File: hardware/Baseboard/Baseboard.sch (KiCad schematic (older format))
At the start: 0 parts

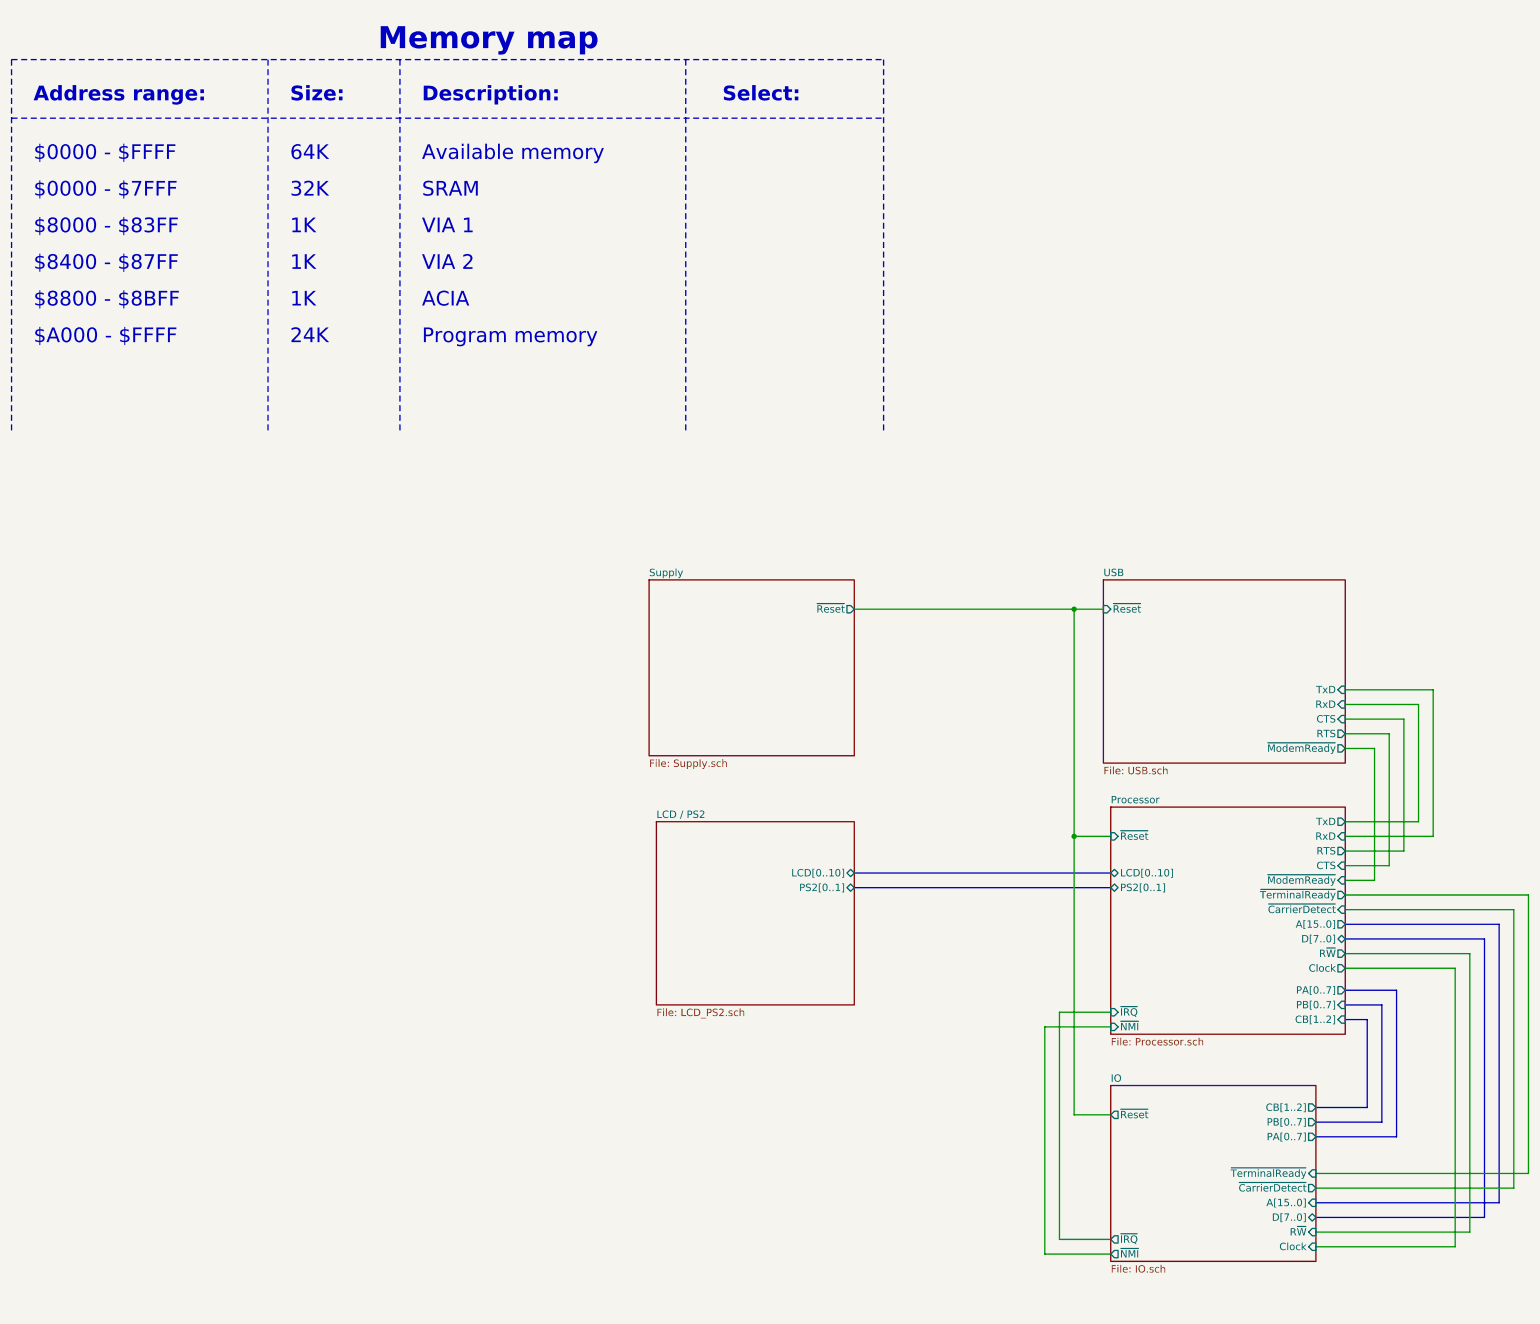
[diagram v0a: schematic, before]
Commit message: Rework hardware for IRQ, change some routing
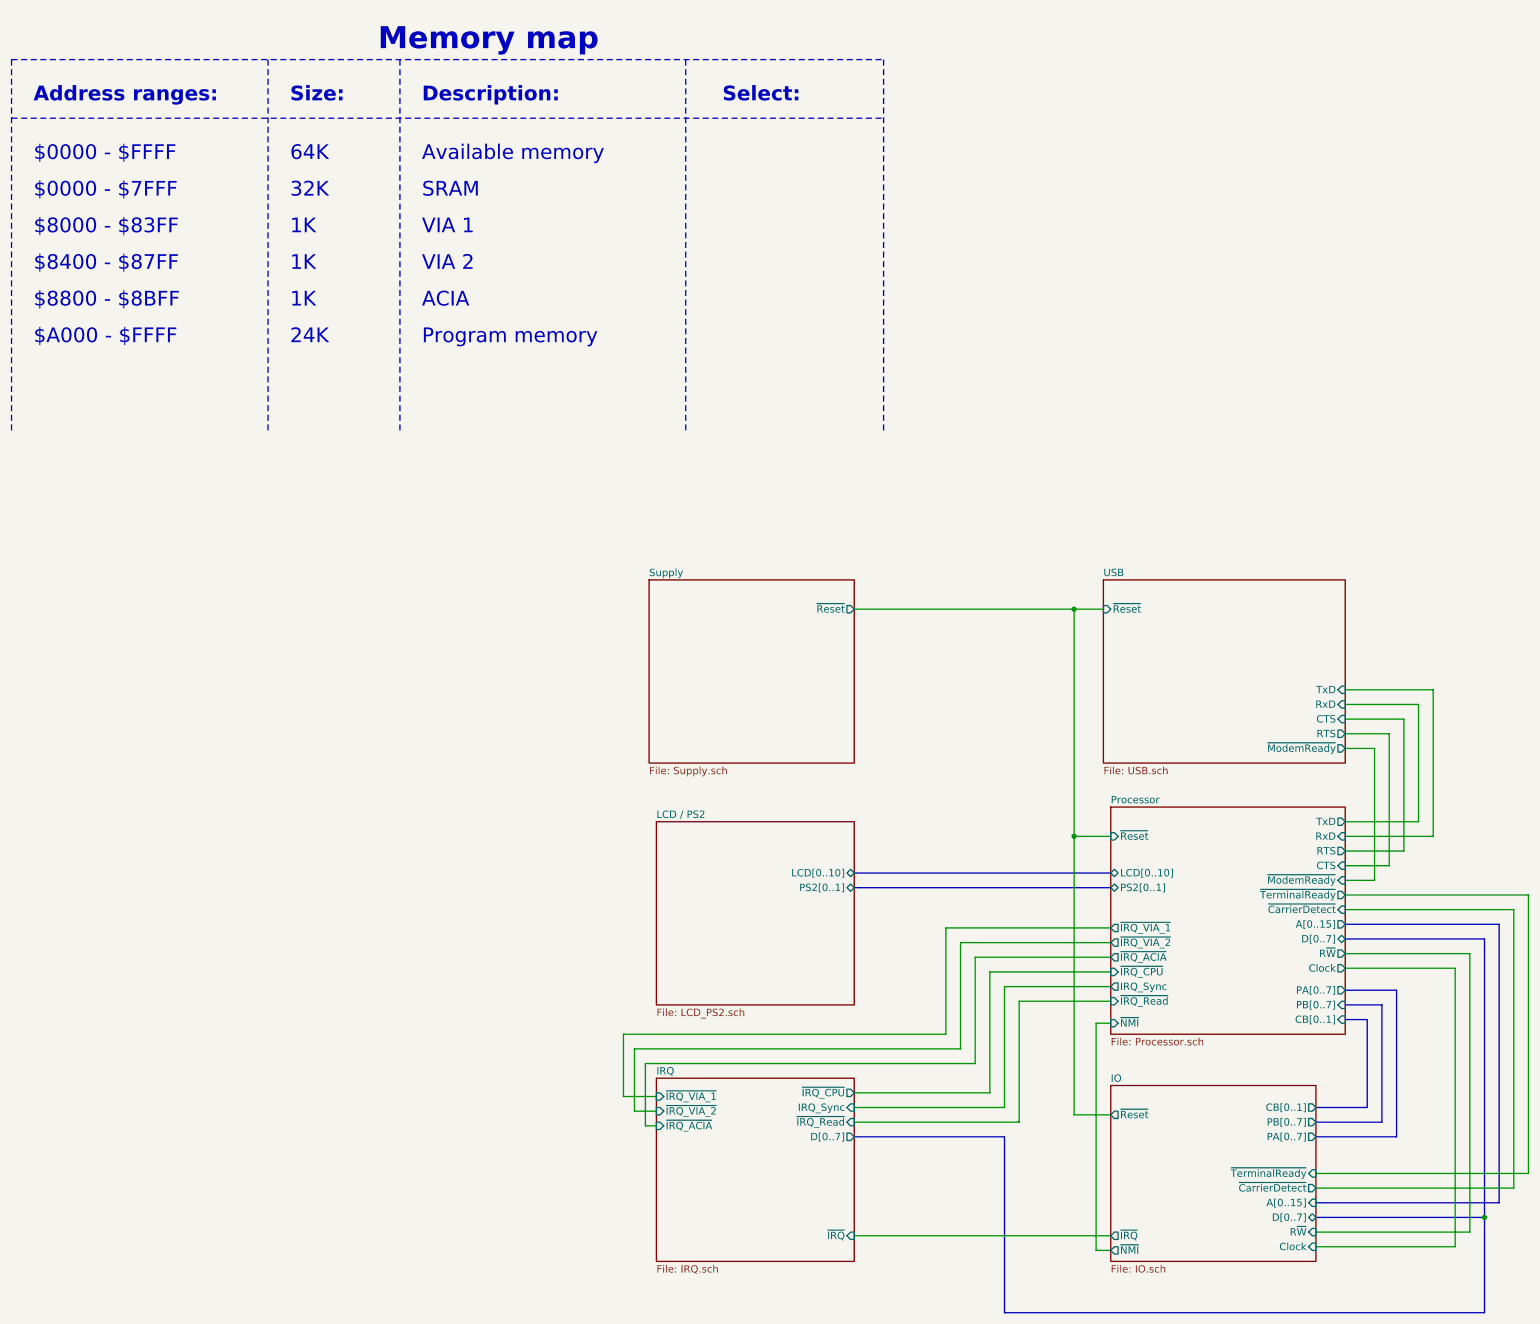
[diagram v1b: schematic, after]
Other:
- note added: "Address ranges:"
- note removed: "Address range:"
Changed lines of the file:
@@
 $Descr A3 16535 11693
 encoding utf-8
-Sheet 1 6
+Sheet 1 7
 Title "Baseboard"
-Date "2019-10-08"
-Rev "1.0"
+Date "2019-11-24"
+Rev "1.1"
 Comp "https://www.kampis-elektroecke.de"
 Comment1 "Author: Daniel Kampert"
@@
 $EndDescr
 Text Notes 900  1450 0    100  ~ 20
-Address range:
+Address ranges:
 Text Notes 3550 1850 0    100  ~ 0
 Available memory
@@
 	8000 4900 8200 4900
 $Sheet
-S 5100 4700 1400 1200
+S 5100 4700 1400 1250
 U 5E9728CC
 F0 "Supply" 50
@@
 F0 "IO" 50
 F1 "IO.sch" 50
-F2 "CB[1..2]" O R 9650 8300 50
-F3 "PB[0..7]" O R 9650 8400 50
-F4 "PA[0..7]" O R 9650 8500 50
-F5 "~NMI" O L 8250 9300 50
-F6 "~IRQ" O L 8250 9200 50
-F7 "R~W" I R 9650 9150 50
-F8 "A[15..0]" I R 9650 8950 50
-F9 "D[7..0]" B R 9650 9050 50
-F10 "Clock" I R 9650 9250 50
-F11 "~TerminalReady" I R 9650 8750 50
-F12 "~CarrierDetect" O R 9650 8850 50
-F13 "~Reset" O L 8250 8350 50
+F2 "PB[0..7]" O R 9650 8400 50
+F3 "PA[0..7]" O R 9650 8500 50
+F4 "~NMI" O L 8250 9275 50
+F5 "~IRQ" O L 8250 9175 50
+F6 "R~W" I R 9650 9150 50
+F7 "Clock" I R 9650 9250 50
+F8 "~TerminalReady" I R 9650 8750 50
+F9 "~CarrierDetect" O R 9650 8850 50
+F10 "~Reset" O L 8250 8350 50
+F11 "CB[0..1]" O R 9650 8300 50
+F12 "A[0..15]" I R 9650 8950 50
+F13 "D[0..7]" B R 9650 9050 50
 $EndSheet
 Text Notes 900  1850 0    100  ~ 0
@@
 24K
 Wire Wire Line
-	7900 7650 8250 7650
-Wire Wire Line
 	10450 5450 10450 6450
 $Sheet
@@
 F1 "Processor.sch" 50
 F2 "PA[0..7]" O R 9850 7500 50
-F3 "CB[1..2]" I R 9850 7700 50
-F4 "PB[0..7]" I R 9850 7600 50
-F5 "TxD" O R 9850 6350 50
-F6 "RxD" I R 9850 6450 50
-F7 "RTS" O R 9850 6550 50
-F8 "CTS" I R 9850 6650 50
-F9 "~NMI" I L 8250 7750 50
-F10 "~IRQ" I L 8250 7650 50
-F11 "R~W" O R 9850 7250 50
-F12 "A[15..0]" O R 9850 7050 50
-F13 "D[7..0]" B R 9850 7150 50
-F14 "LCD[0..10]" B L 8250 6700 50
-F15 "PS2[0..1]" B L 8250 6800 50
-F16 "~ModemReady" I R 9850 6750 50
-F17 "Clock" O R 9850 7350 50
-F18 "~TerminalReady" O R 9850 6850 50
-F19 "~CarrierDetect" I R 9850 6950 50
-F20 "~Reset" I L 8250 6450 50
+F3 "PB[0..7]" I R 9850 7600 50
+F4 "TxD" O R 9850 6350 50
+F5 "RxD" I R 9850 6450 50
+F6 "RTS" O R 9850 6550 50
+F7 "CTS" I R 9850 6650 50
+F8 "~NMI" I L 8250 7725 50
+F9 "R~W" O R 9850 7250 50
+F10 "LCD[0..10]" B L 8250 6700 50
+F11 "PS2[0..1]" B L 8250 6800 50
+F12 "~ModemReady" I R 9850 6750 50
+F13 "Clock" O R 9850 7350 50
+F14 "~TerminalReady" O R 9850 6850 50
+F15 "~CarrierDetect" I R 9850 6950 50
+F16 "~Reset" I L 8250 6450 50
+F17 "~IRQ_VIA_2" O L 8250 7175 50
+F18 "~IRQ_VIA_1" O L 8250 7075 50
+F19 "~IRQ_ACIA" O L 8250 7275 50
+F20 "~IRQ_CPU" I L 8250 7375 50
+F21 "IRQ_Sync" O L 8250 7475 50
+F22 "~IRQ_Read" I L 8250 7575 50
+F23 "CB[0..1]" I R 9850 7700 50
+F24 "A[0..15]" O R 9850 7050 50
+F25 "D[0..7]" B R 9850 7150 50
 $EndSheet
 Wire Bus Line
@@
 Wire Bus Line
 	9850 7050 10900 7050
-Wire Wire Line
-	7800 7750 8250 7750
 Wire Bus Line
 	9650 8400 10100 8400
@@
 Wire Wire Line
 	11000 6950 9850 6950
-Wire Wire Line
-	8250 9200 7900 9200
-Wire Wire Line
-	8250 9300 7800 9300
-Wire Wire Line
-	7800 7750 7800 9300
-Wire Wire Line
-	7900 7650 7900 9200
+$Sheet
+S 5150 8100 1350 1250
+U 5E710B5B
+F0 "IRQ" 50
+F1 "IRQ.sch" 50
+F2 "~IRQ" I R 6500 9175 50
+F3 "~IRQ_VIA_1" I L 5150 8225 50
+F4 "~IRQ_VIA_2" I L 5150 8325 50
+F5 "~IRQ_ACIA" I L 5150 8425 50
+F6 "~IRQ_CPU" O R 6500 8200 50
+F7 "IRQ_Sync" I R 6500 8300 50
+F8 "~IRQ_Read" I R 6500 8400 50
+F9 "D[0..7]" O R 6500 8500 50
+$EndSheet
+Wire Wire Line
+	8250 7375 7425 7375
+Wire Wire Line
+	8250 7475 7525 7475
+Wire Bus Line
+	10800 9050 10800 9700
+Wire Bus Line
+	10800 9700 7525 9700
+Wire Bus Line
+	7525 9700 7525 8500
+Connection ~ 10800 9050
+Wire Wire Line
+	8250 7075 7125 7075
+Wire Wire Line
+	7125 7075 7125 7800
+Wire Wire Line
+	7125 7800 4925 7800
+Wire Wire Line
+	8250 7175 7225 7175
+Wire Wire Line
+	7225 7175 7225 7900
+Wire Wire Line
+	7225 7900 5000 7900
+Wire Wire Line
+	8250 7275 7325 7275
+Wire Wire Line
+	7325 7275 7325 8000
+Wire Wire Line
+	7325 8000 5075 8000
+Wire Wire Line
+	7625 7575 8250 7575
+Wire Wire Line
+	8250 7725 8150 7725
+Wire Wire Line
+	8150 7725 8150 9275
+Wire Wire Line
+	8250 9275 8150 9275
+Wire Wire Line
+	8250 9175 6500 9175
+Wire Bus Line
+	6500 8500 7525 8500
+Wire Wire Line
+	6500 8400 7625 8400
+Wire Wire Line
+	6500 8300 7525 8300
+Wire Wire Line
+	6500 8200 7425 8200
+Wire Wire Line
+	7425 7375 7425 8200
+Wire Wire Line
+	7525 7475 7525 8300
+Wire Wire Line
+	7625 7575 7625 8400
+Wire Wire Line
+	5150 8425 5075 8425
+Wire Wire Line
+	5150 8325 5000 8325
+Wire Wire Line
+	4925 8225 5150 8225
+Wire Wire Line
+	5000 7900 5000 8325
+Wire Wire Line
+	5075 8000 5075 8425
+Wire Wire Line
+	4925 7800 4925 8225
 $EndSCHEMATC

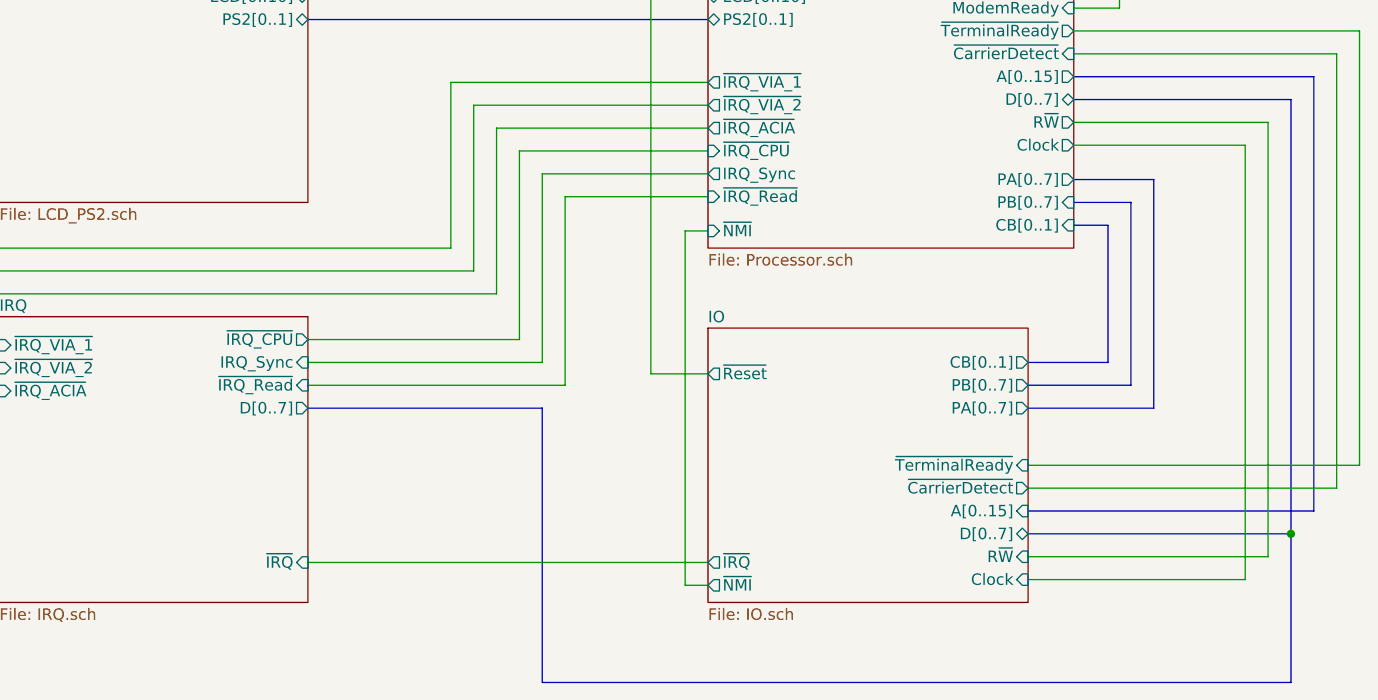
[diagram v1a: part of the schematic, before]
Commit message: Improve routing, add some datasheet recommendations
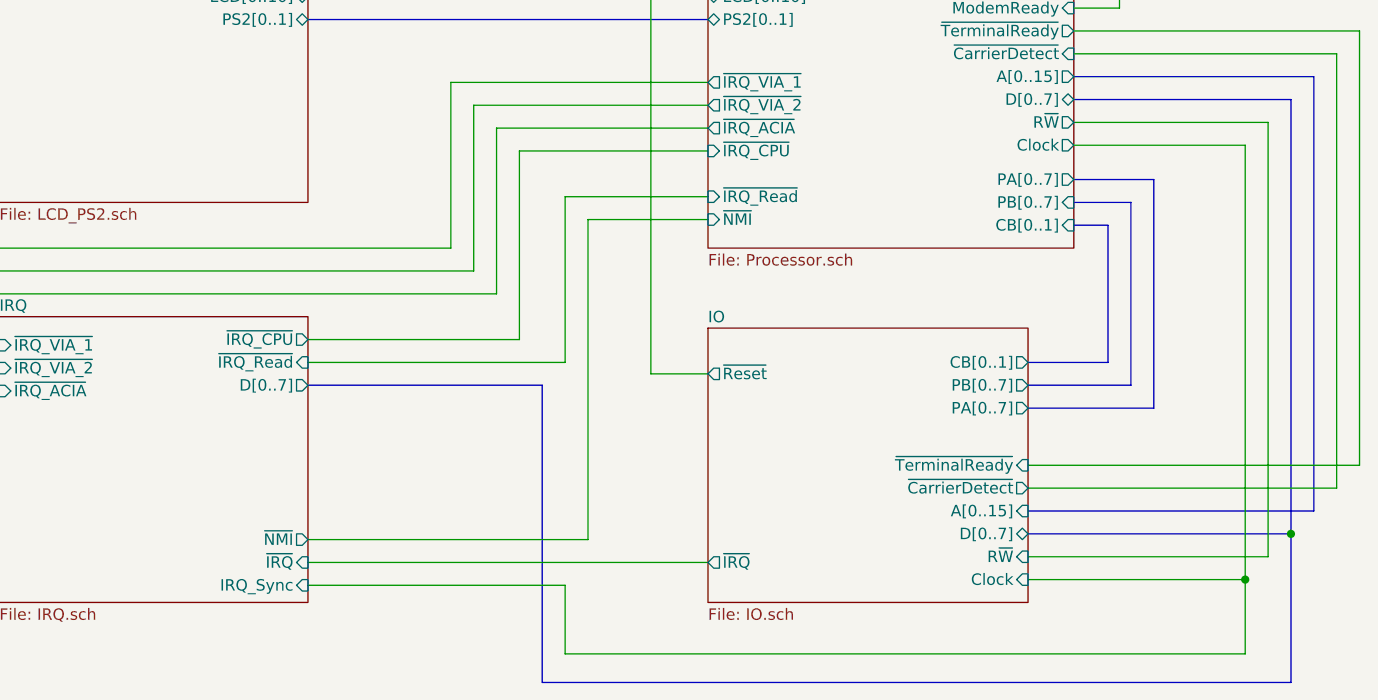
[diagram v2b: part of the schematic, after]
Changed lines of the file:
@@
 F2 "PB[0..7]" O R 9650 8400 50
 F3 "PA[0..7]" O R 9650 8500 50
-F4 "~NMI" O L 8250 9275 50
-F5 "~IRQ" O L 8250 9175 50
-F6 "R~W" I R 9650 9150 50
-F7 "Clock" I R 9650 9250 50
-F8 "~TerminalReady" I R 9650 8750 50
-F9 "~CarrierDetect" O R 9650 8850 50
-F10 "~Reset" O L 8250 8350 50
-F11 "CB[0..1]" O R 9650 8300 50
-F12 "A[0..15]" I R 9650 8950 50
-F13 "D[0..7]" B R 9650 9050 50
+F4 "~IRQ" O L 8250 9175 50
+F5 "R~W" I R 9650 9150 50
+F6 "Clock" I R 9650 9250 50
+F7 "~TerminalReady" I R 9650 8750 50
+F8 "~CarrierDetect" O R 9650 8850 50
+F9 "~Reset" O L 8250 8350 50
+F10 "CB[0..1]" O R 9650 8300 50
+F11 "A[0..15]" I R 9650 8950 50
+F12 "D[0..7]" B R 9650 9050 50
 $EndSheet
 Text Notes 900  1850 0    100  ~ 0
@@
 F6 "RTS" O R 9850 6550 50
 F7 "CTS" I R 9850 6650 50
-F8 "~NMI" I L 8250 7725 50
+F8 "~NMI" I L 8250 7675 50
 F9 "R~W" O R 9850 7250 50
 F10 "LCD[0..10]" B L 8250 6700 50
@@
 F19 "~IRQ_ACIA" O L 8250 7275 50
 F20 "~IRQ_CPU" I L 8250 7375 50
-F21 "IRQ_Sync" O L 8250 7475 50
-F22 "~IRQ_Read" I L 8250 7575 50
-F23 "CB[0..1]" I R 9850 7700 50
-F24 "A[0..15]" O R 9850 7050 50
-F25 "D[0..7]" B R 9850 7150 50
+F21 "~IRQ_Read" I L 8250 7575 50
+F22 "CB[0..1]" I R 9850 7700 50
+F23 "A[0..15]" O R 9850 7050 50
+F24 "D[0..7]" B R 9850 7150 50
 $EndSheet
 Wire Bus Line
@@
 F5 "~IRQ_ACIA" I L 5150 8425 50
 F6 "~IRQ_CPU" O R 6500 8200 50
-F7 "IRQ_Sync" I R 6500 8300 50
-F8 "~IRQ_Read" I R 6500 8400 50
-F9 "D[0..7]" O R 6500 8500 50
+F7 "IRQ_Sync" I R 6500 9275 50
+F8 "~IRQ_Read" I R 6500 8300 50
+F9 "D[0..7]" O R 6500 8400 50
+F10 "~NMI" O R 6500 9075 50
 $EndSheet
 Wire Wire Line
 	8250 7375 7425 7375
-Wire Wire Line
-	8250 7475 7525 7475
 Wire Bus Line
 	10800 9050 10800 9700
 Wire Bus Line
 	10800 9700 7525 9700
-Wire Bus Line
-	7525 9700 7525 8500
 Connection ~ 10800 9050
 Wire Wire Line
@@
 	7625 7575 8250 7575
 Wire Wire Line
-	8250 7725 8150 7725
-Wire Wire Line
-	8150 7725 8150 9275
-Wire Wire Line
-	8250 9275 8150 9275
-Wire Wire Line
 	8250 9175 6500 9175
-Wire Bus Line
-	6500 8500 7525 8500
-Wire Wire Line
-	6500 8400 7625 8400
-Wire Wire Line
-	6500 8300 7525 8300
 Wire Wire Line
 	6500 8200 7425 8200
@@
 	7425 7375 7425 8200
 Wire Wire Line
-	7525 7475 7525 8300
-Wire Wire Line
-	7625 7575 7625 8400
+	7625 7575 7625 8300
 Wire Wire Line
 	5150 8425 5075 8425
@@
 Wire Wire Line
 	4925 7800 4925 8225
+Wire Wire Line
+	6500 9075 7725 9075
+Wire Wire Line
+	8250 7675 7725 7675
+Wire Wire Line
+	7725 7675 7725 9075
+Wire Bus Line
+	6500 8400 7525 8400
+Wire Bus Line
+	7525 8400 7525 9700
+Wire Wire Line
+	6500 8300 7625 8300
+Wire Wire Line
+	10600 9250 10600 9575
+Wire Wire Line
+	10600 9575 7625 9575
+Wire Wire Line
+	7625 9575 7625 9275
+Wire Wire Line
+	7625 9275 6500 9275
+Connection ~ 10600 9250
 $EndSCHEMATC
